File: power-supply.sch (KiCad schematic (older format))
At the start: 99 parts, among them IC1 TPS54561, J12 S2B-PH-K-S_LF__SN_, Q10 2N7002, Q11 2N7002, Q7 2N7002, Q8 2N7002, Q9 2N7002, U10 TPS62823DLCT, U11 TPS62823DLCT, U12 TPS62823DLCT, U13 TPS62823DLCT, U9 LM3881MME_NOPB

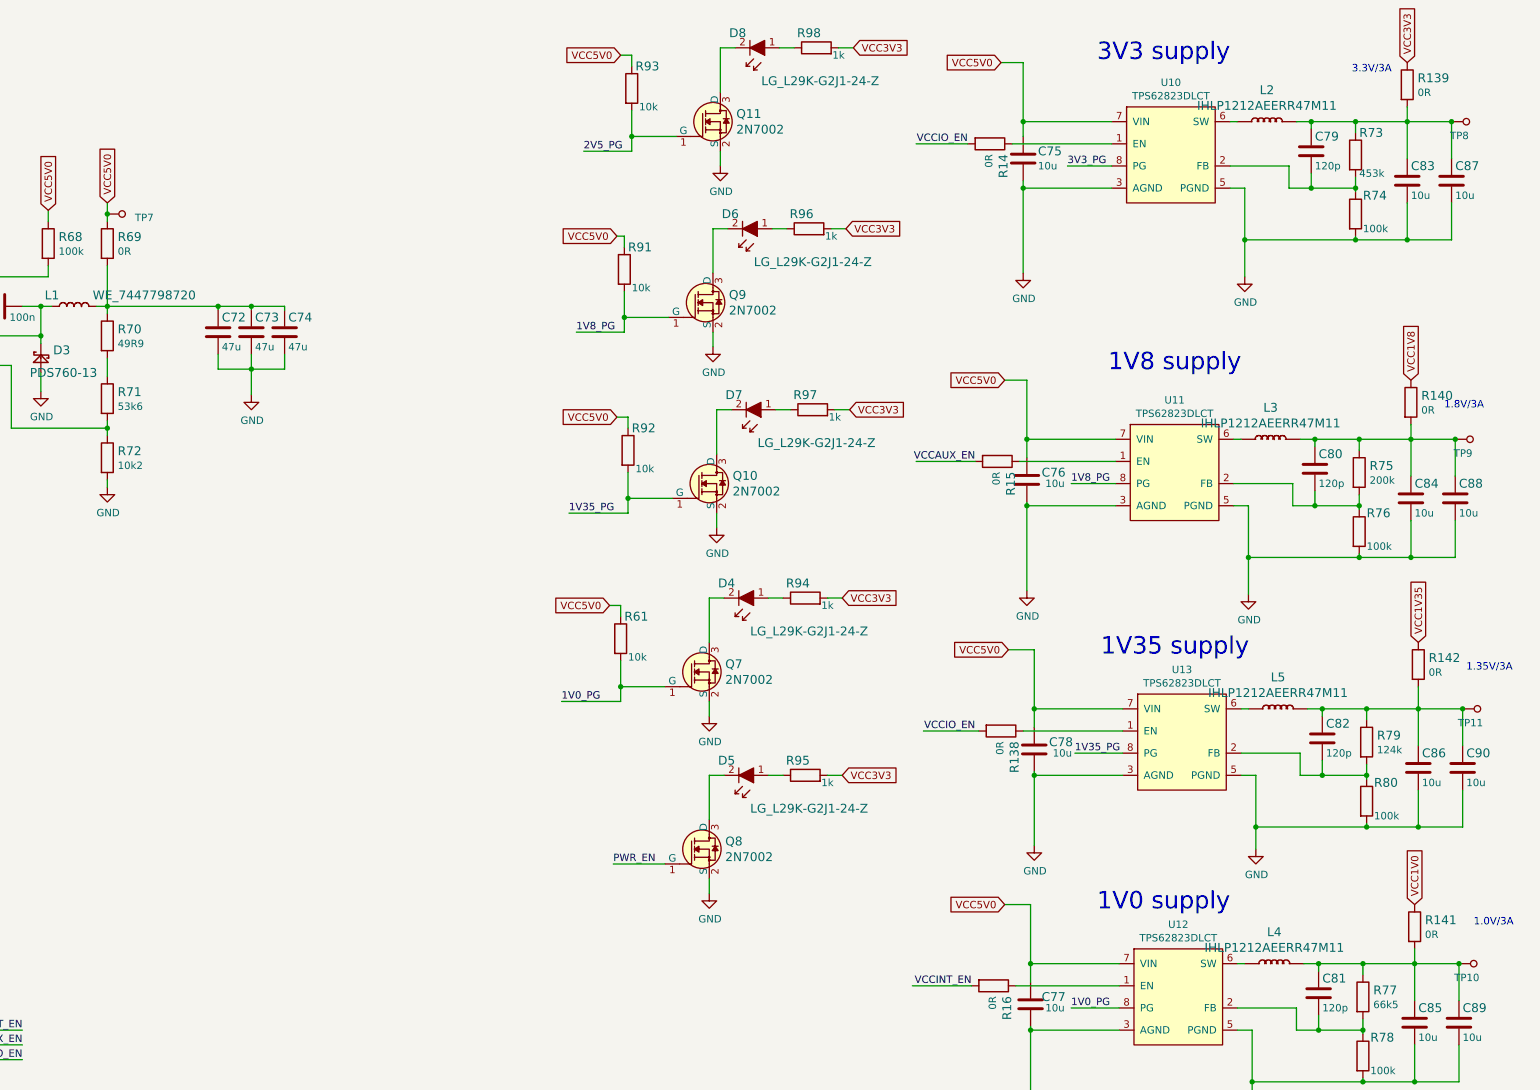
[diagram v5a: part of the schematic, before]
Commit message: Update layout around DC/dC
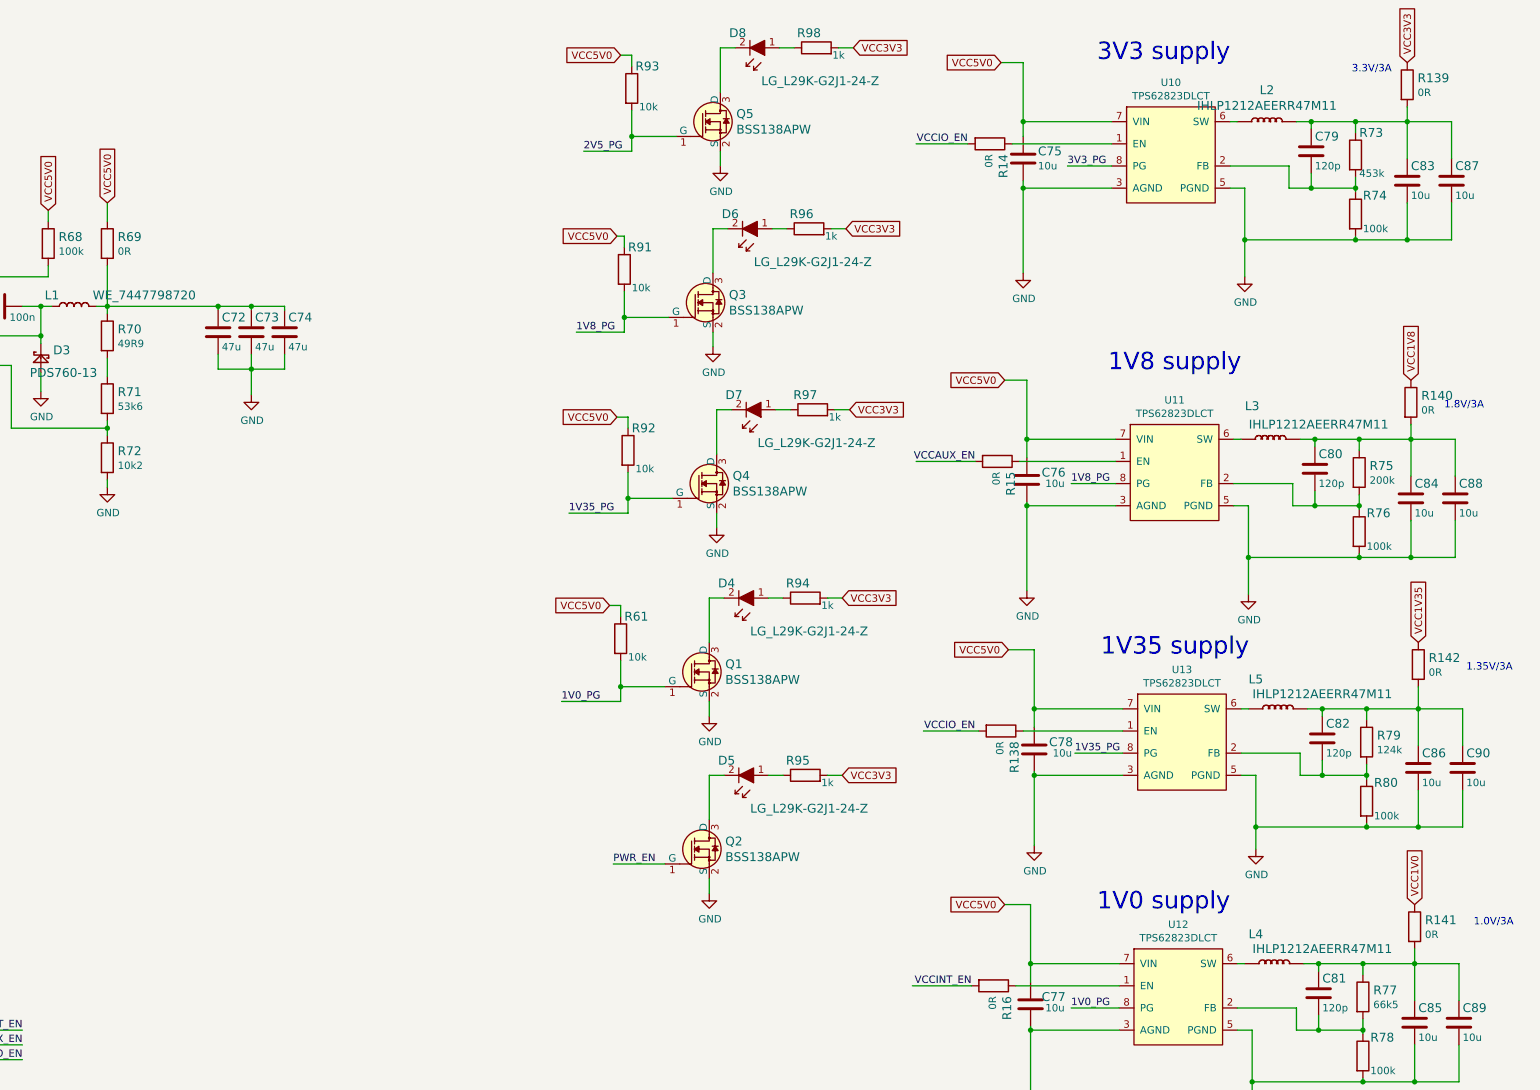
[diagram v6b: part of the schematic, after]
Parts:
- removed L2, L3, L4, L5: IHLP1212AEERR47M11, artix-dc-scm-footprints:IHLP-1212AE, symbol artix-dc-scm:IHLP1212AEERR47M11
- removed Q10, Q11, Q7, Q8, Q9: 2N7002, artix-dc-scm-footprints:SOT-23-3, symbol artix-dc-scm:2N7002
- removed R139, R140, R141, R142: R_0R_1206, artix-dc-scm-footprints:1206-res, symbol artix-dc-scm:R_0R_1206
- removed TP10, TP11, TP7, TP8, TP9: TP_SMD1MM, artix-dc-scm-footprints:Testpoint_smd_1mm, symbol artix-dc-scm:TP_SMD1MM
- added L2, L3, L4, L5: IHLP1212AEERR47M11, antmicro-footprints:IHLP-1212AE, symbol antmicroFixedInductors:IHLP1212AEERR47M11
- added Q1, Q2, Q3, Q4, Q5: BSS138APW, antmicro-footprints:SC70-3, symbol antmicroTransistorsFETsMOSFETsSingle:BSS138APW
- added R139, R140, R141, R142: R_0R_0603, antmicro-footprints:0603-res, symbol antmicroResistors0603:R_0R_0603
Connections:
- net 1V0_PG: now also Q1.1 (G)
- net 1V35_PG: now also Q4.1 (G)
- net 1V8_PG: now also Q3.1 (G)
- net 2V5_PG: now also Q5.1 (G)
- net GND: now also Q1.2 (S), Q2.2 (S), Q3.2 (S), Q4.2 (S), Q5.2 (S)
- net PWR_EN: now also Q2.1 (G)
- net VCC1V0: now also R141.1
- net VCC1V35: now also R142.1
- net VCC1V8: now also R140.1
- net VCC3V3: now also R139.1
- net at C79.1, C83.1, C87.1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: now also L2.2 (P), R139.2
- net at C80.1, C84.1, C88.1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: now also L3.2 (P), R140.2
- net at C82.1, C86.1, C90.1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: now also L5.2 (P), R142.2
- net at C81.1, C85.1, C89.1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: now also L4.2 (P), R141.2
- net at D8.2: now also Q5.3 (D)
- net at D6.2: now also Q3.3 (D)
- net at D7.2: now also Q4.3 (D)
- net at D4.2: now also Q1.3 (D)
- net at D5.2: now also Q2.3 (D)
- net at U10.6 (SW): now also L2.1 (P)
- net at U11.6 (SW): now also L3.1 (P)
- net at U13.6 (SW): now also L5.1 (P)
- net at U12.6 (SW): now also L4.1 (P)

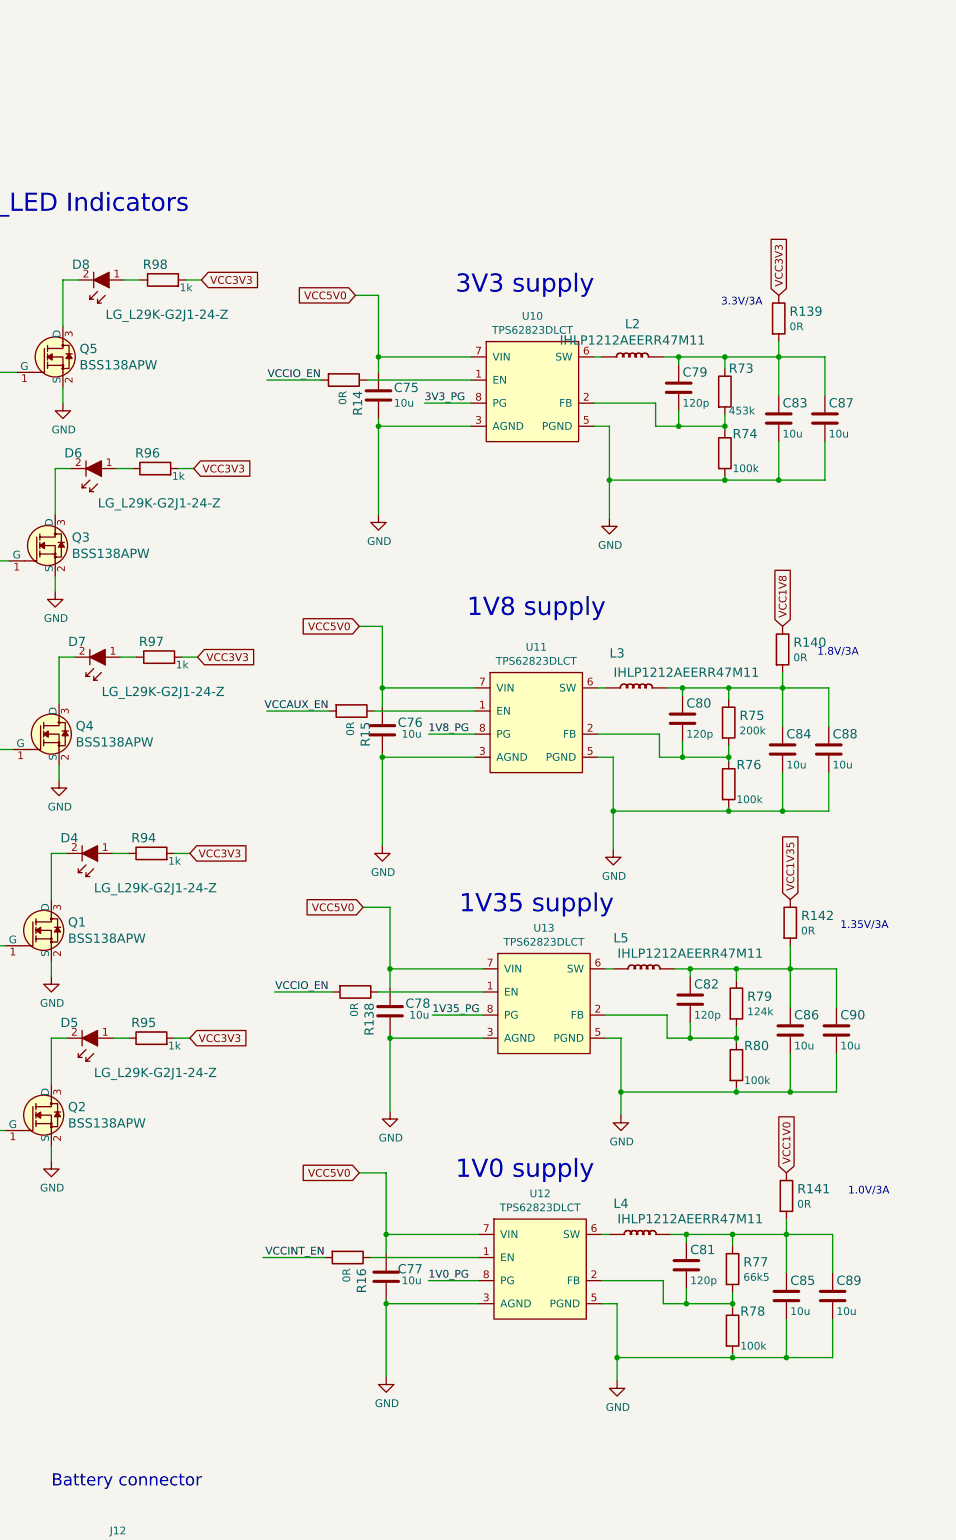
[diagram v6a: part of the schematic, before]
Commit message: Replaced 1V2 voltage regulator
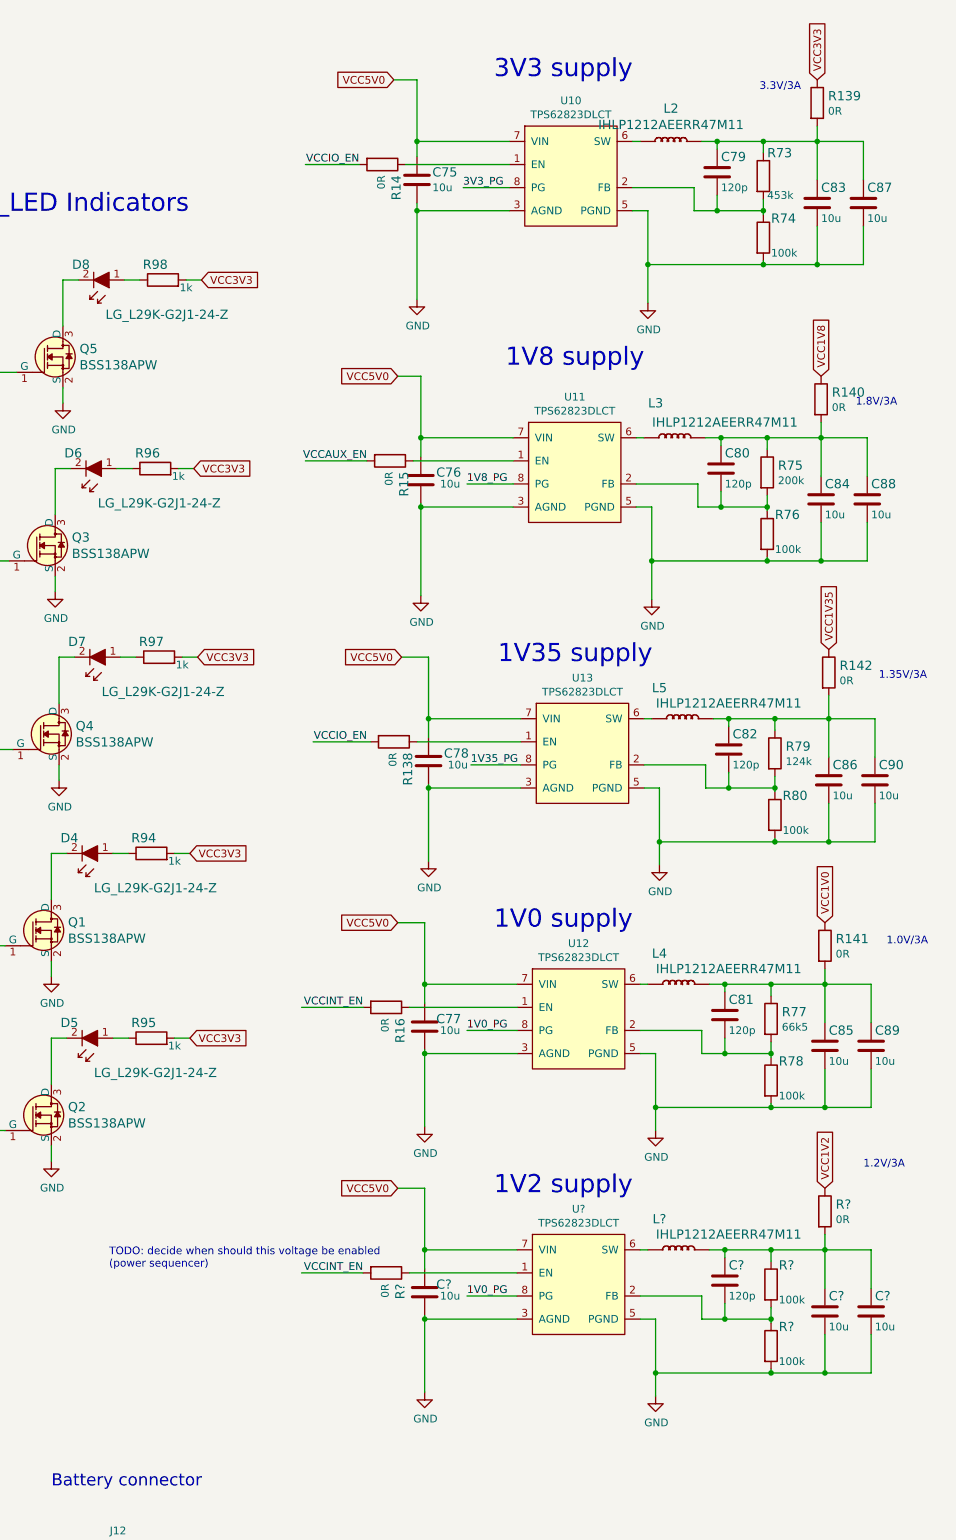
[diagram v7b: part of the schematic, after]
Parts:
- added C? (x3): C_10u_0402, artix-dc-scm-footprints:0402-cap, symbol artix-dc-scm:C_10u_0402
- added C?: C_120p_0402, artix-dc-scm-footprints:0402-res, symbol artix-dc-scm:C_120p_0402
- added L?: IHLP1212AEERR47M11, antmicro-footprints:IHLP-1212AE, symbol antmicroFixedInductors:IHLP1212AEERR47M11
- added R? (x2): R_100k_0402, artix-dc-scm-footprints:0402-res, symbol artix-dc-scm:R_100k_0402
- added R?: R_0R_0402, artix-dc-scm-footprints:0402-res, symbol artix-dc-scm:R_0R_0402
- added R?: R_0R_0603, antmicro-footprints:0603-res, symbol antmicroResistors0603:R_0R_0603
- added U?: TPS62823DLCT, artix-dc-scm-footprints:QFN-8_2x1mm, symbol artix-dc-scm:TPS62823DLCT
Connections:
- net 1V0_PG: now also U?.8 (PG)
- net GND: now also C?.2, C?.2, C?.2, R?.2, U?.3 (AGND), U?.5 (PGND)
- net VCC5V0: now also C?.1, U?.7 (VIN)
- net VCCINT_EN: now also R?.2
- new net: R?.1, U?.1 (EN)
- new net: C?.2, R?.1, R?.2, U?.2 (FB)
- new net: L?.1 (P), U?.6 (SW)
- new net: C?.1, C?.1, C?.1, L?.2 (P), R?.1, R?.2
- new net VCC1V2: R?.1
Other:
- note added: "1.2V/3A"
- note added: "1V2 supply"
- note added: "TODO: decide when should this voltage be enabled\n(power sequencer)"
- moved on the sheet: C75, C76, C77, C78, C79, C80, C81, C82, C83, C84, C85, C86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
